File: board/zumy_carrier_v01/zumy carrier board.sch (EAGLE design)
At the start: 17 parts, among them M1 POLOLU_STEP_DOWN, M2 ITG/MPU_MODULE, M3 POLOLU_DRV8833_MODULE, SW1 500SSP1S1M6QEA

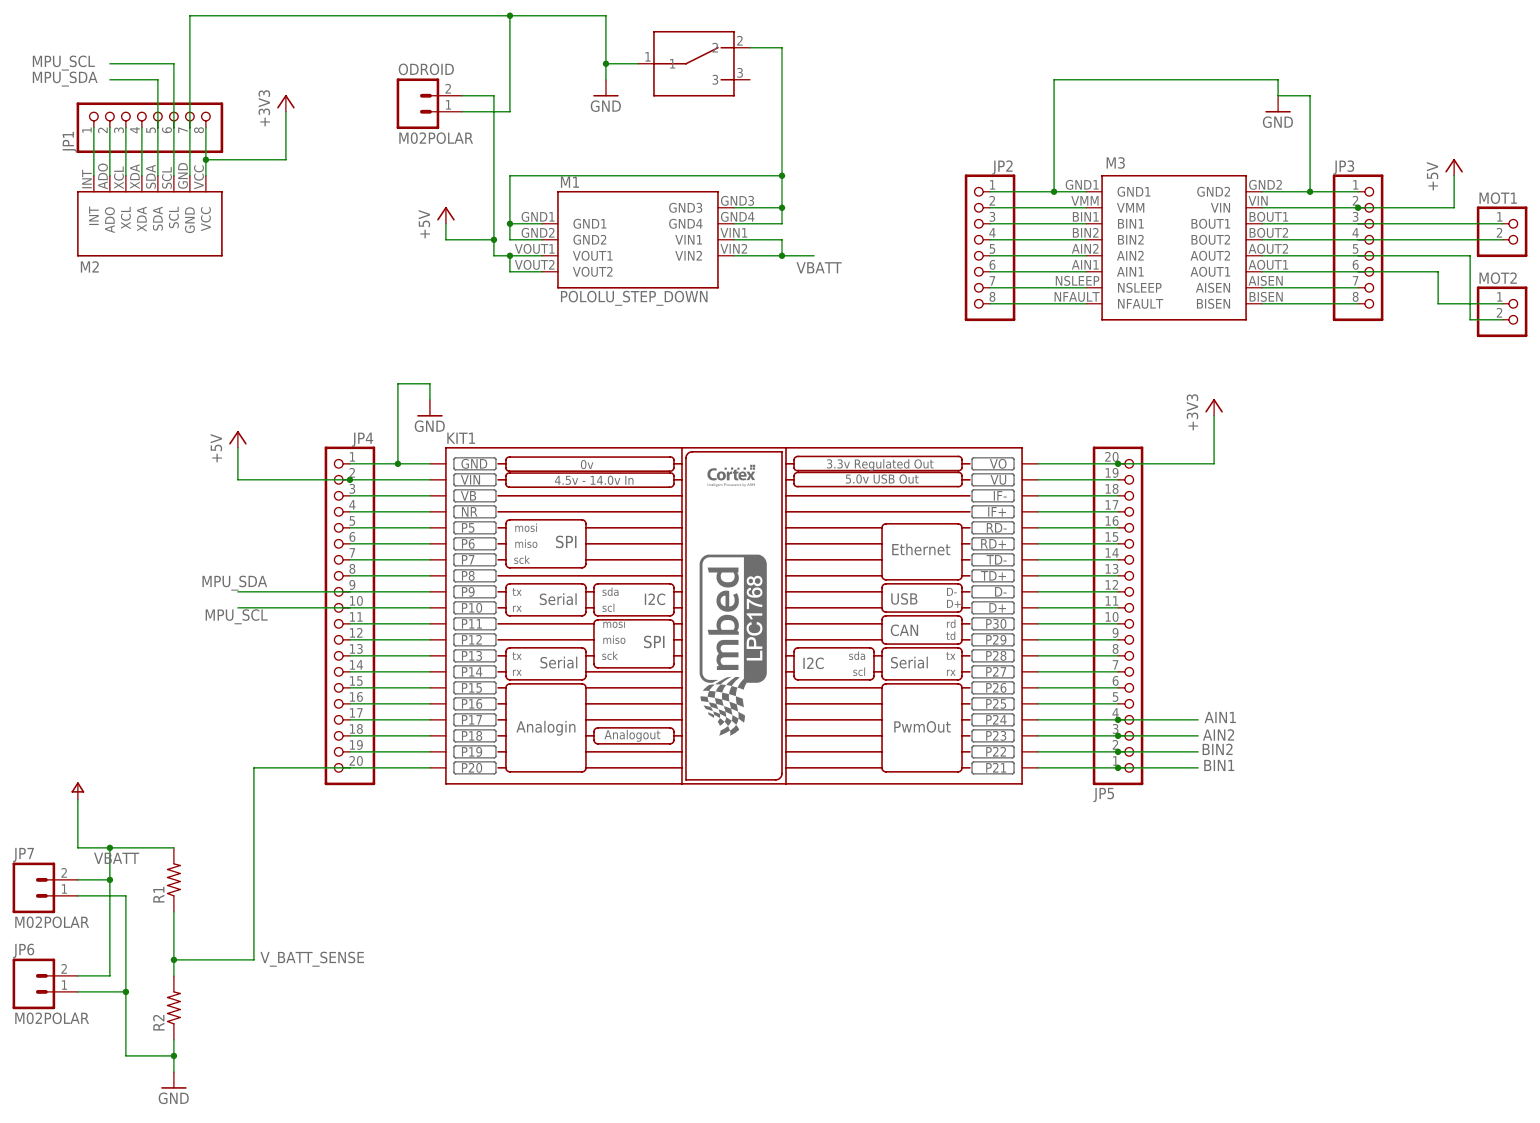
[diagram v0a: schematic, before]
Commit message: Preliminary updates for rev c, unrouted.
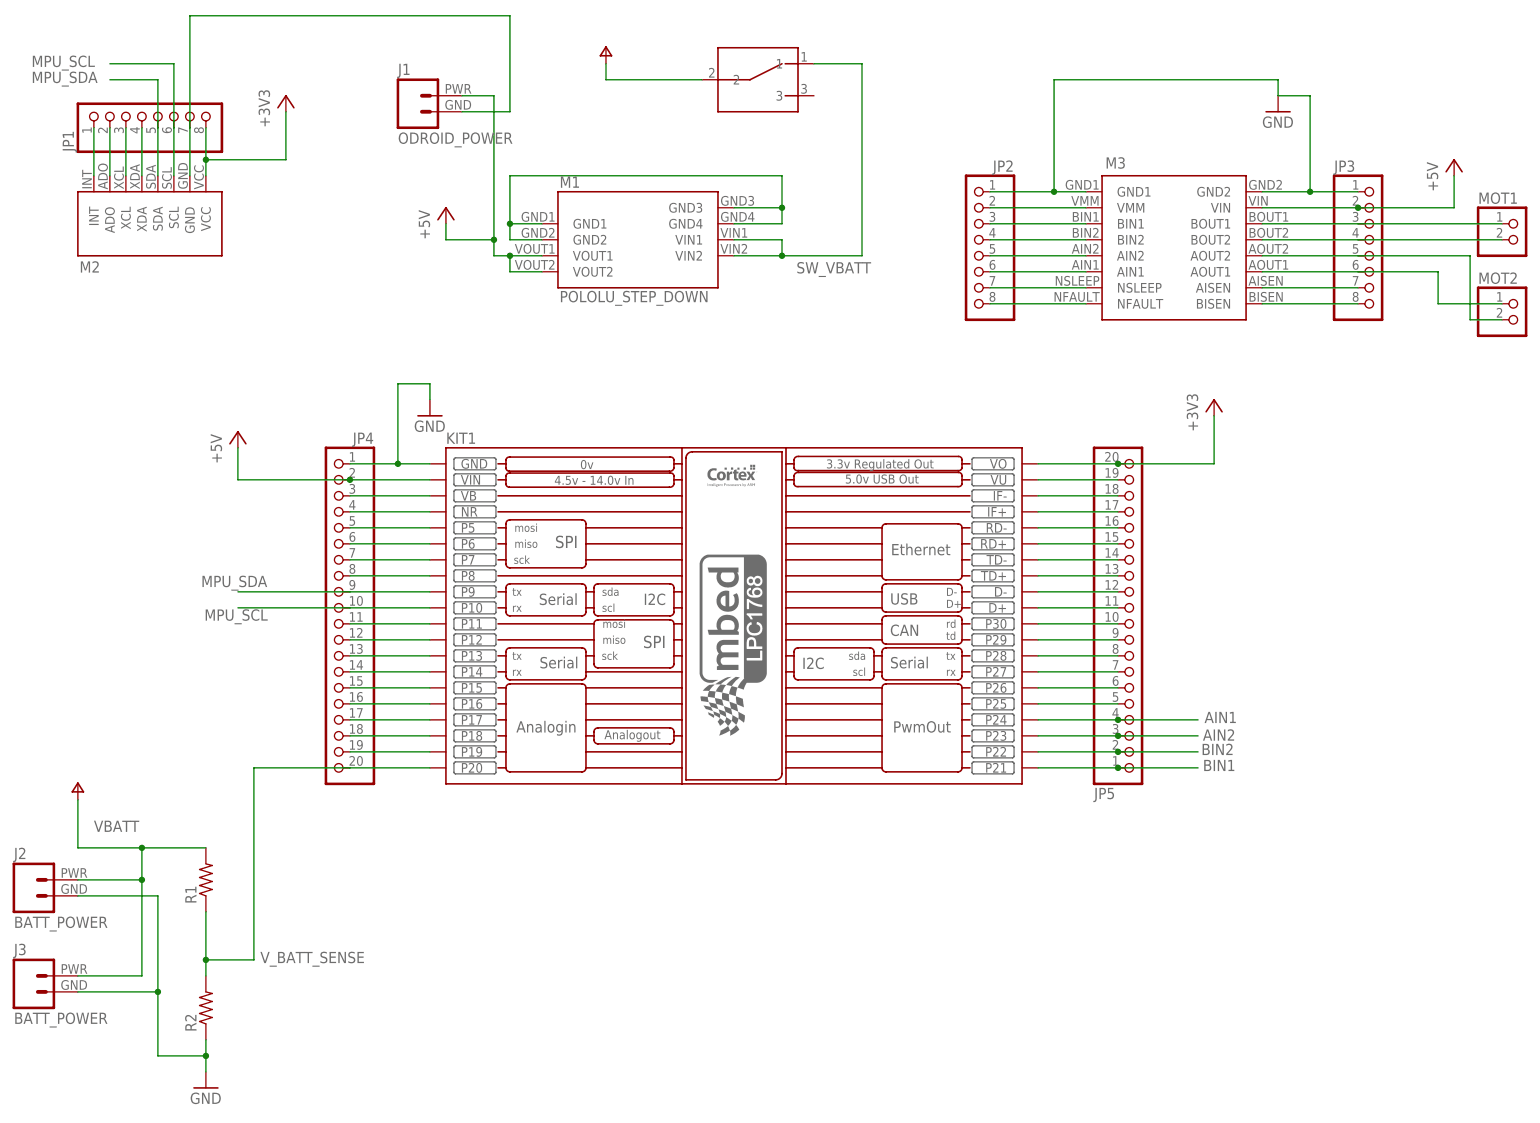
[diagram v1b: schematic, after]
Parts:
- removed JP6, JP7, ODROID: M02POLAR, SparkFun-Connectors:M02POLAR
- added J1: ODROID_POWER, zumy:ODROID_POWER
- added J2, J3: BATT_POWER, zumy:BATT_POWER
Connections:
- new net N$5: J1.GND, JP1.7, M2.GND
- new net SW_VBATT: M1.VIN1, M1.VIN2, SW1.1
- net +5V: now also J1.PWR; no longer ODROID.2
- net GND: now also J2.GND, J3.GND; no longer JP1.7, JP6.1, JP7.1, M2.GND, ODROID.1, SW1.1
- net N$65: no longer SW1.2
- net VBATT: now also J2.PWR, J3.PWR, SW1.2; no longer JP6.2, JP7.2, M1.VIN1, M1.VIN2
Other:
- moved on the sheet: R1, R2

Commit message: added rev c zumy carrier board
expanded odroid power holes
expanded battery power holes
module layout change
fixed switching cicuit to switch battery rather than ground
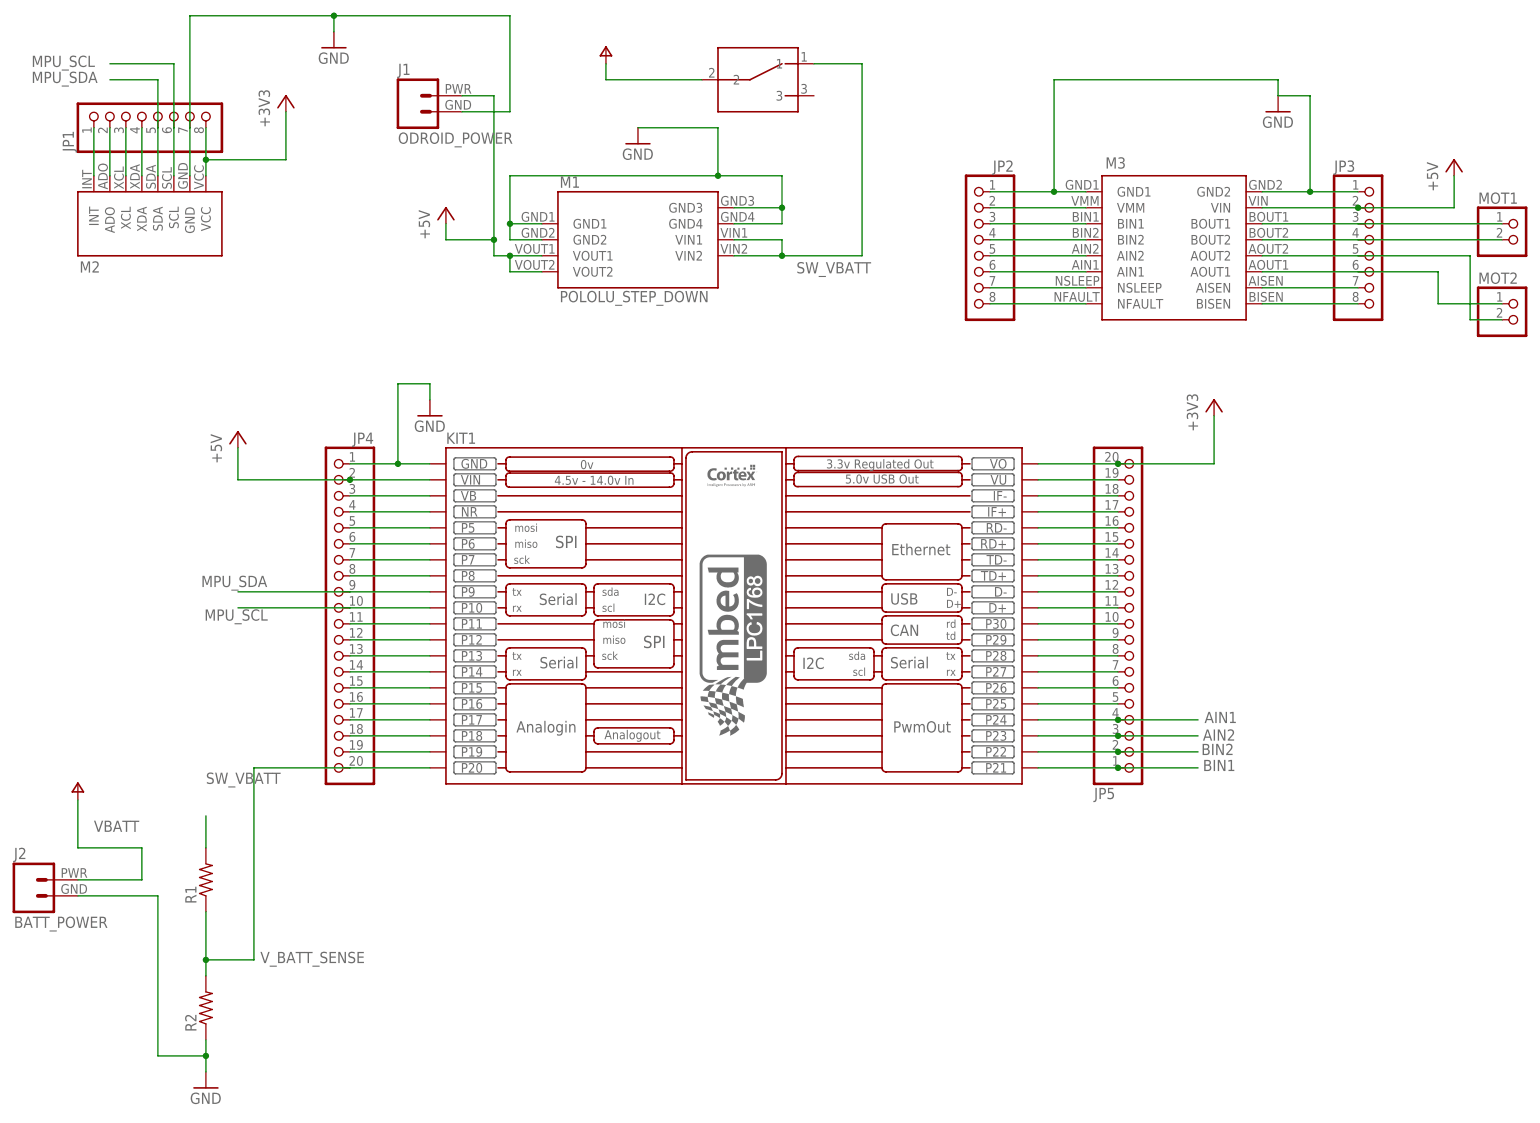
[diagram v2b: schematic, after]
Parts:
- removed J3: BATT_POWER, zumy:BATT_POWER
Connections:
- removed net N$5: J1.GND, JP1.7, M2.GND
- removed net N$65: M1.GND1, M1.GND2, M1.GND3, M1.GND4
- net GND: now also J1.GND, JP1.7, M1.GND1, M1.GND2, M1.GND3, M1.GND4, M2.GND; no longer J3.GND
- net SW_VBATT: now also R1.2
- net VBATT: no longer J3.PWR, R1.2
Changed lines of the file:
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@@
 <?xml version="1.0" encoding="utf-8"?>
 <!DOCTYPE eagle SYSTEM "eagle.dtd">
-<eagle version="6.5.0">
+<eagle version="6.6.0">
 <drawing>
 <settings>
@@
 <part name="P+5" library="supply1" deviceset="V+" device=""/>
 <part name="J2" library="zumy" deviceset="BATT_POWER" device=""/>
-<part name="J3" library="zumy" deviceset="BATT_POWER" device=""/>
+<part name="GND3" library="supply1" deviceset="GND" device=""/>
+<part name="GND5" library="supply1" deviceset="GND" device=""/>
 </parts>
 <sheets>
@@
 <instance part="P+5" gate="1" x="99.06" y="172.72" smashed="yes"/>
 <instance part="J2" gate="G$1" x="5.08" y="35.56"/>
-<instance part="J3" gate="G$1" x="5.08" y="20.32"/>
+<instance part="GND3" gate="1" x="104.14" y="157.48"/>
+<instance part="GND5" gate="1" x="55.88" y="172.72"/>
 </instances>
 <busses>
@@
 <pinref part="JP3" gate="A" pin="8"/>
 <wire x1="203.2" y1="132.08" x2="218.44" y2="132.08" width="0.1524" layer="91"/>
-</segment>
-</net>
-<net name="N$65" class="0">
-<segment>
-<pinref part="M1" gate="G$1" pin="GND3"/>
-<wire x1="127" y1="152.4" x2="127" y2="147.32" width="0.1524" layer="91"/>
-<wire x1="127" y1="147.32" x2="119.38" y2="147.32" width="0.1524" layer="91"/>
-<wire x1="127" y1="147.32" x2="127" y2="144.78" width="0.1524" layer="91"/>
-<pinref part="M1" gate="G$1" pin="GND4"/>
-<wire x1="127" y1="144.78" x2="119.38" y2="144.78" width="0.1524" layer="91"/>
-<junction x="127" y="147.32"/>
-<pinref part="M1" gate="G$1" pin="GND1"/>
-<wire x1="88.9" y1="144.78" x2="83.82" y2="144.78" width="0.1524" layer="91"/>
-<pinref part="M1" gate="G$1" pin="GND2"/>
-<wire x1="88.9" y1="142.24" x2="83.82" y2="142.24" width="0.1524" layer="91"/>
-<wire x1="83.82" y1="142.24" x2="83.82" y2="144.78" width="0.1524" layer="91"/>
-<wire x1="83.82" y1="144.78" x2="83.82" y2="152.4" width="0.1524" layer="91"/>
-<wire x1="83.82" y1="152.4" x2="127" y2="152.4" width="0.1524" layer="91"/>
-<junction x="83.82" y="144.78"/>
 </segment>
 </net>
@@
 <pinref part="GND1" gate="1" pin="GND"/>
 <wire x1="35.56" y1="12.7" x2="35.56" y2="10.16" width="0.1524" layer="91"/>
-<wire x1="15.24" y1="22.86" x2="27.94" y2="22.86" width="0.1524" layer="91"/>
-<wire x1="27.94" y1="22.86" x2="27.94" y2="12.7" width="0.1524" layer="91"/>
 <wire x1="27.94" y1="12.7" x2="35.56" y2="12.7" width="0.1524" layer="91"/>
 <junction x="35.56" y="12.7"/>
 <wire x1="15.24" y1="38.1" x2="27.94" y2="38.1" width="0.1524" layer="91"/>
-<wire x1="27.94" y1="38.1" x2="27.94" y2="22.86" width="0.1524" layer="91"/>
-<junction x="27.94" y="22.86"/>
+<wire x1="27.94" y1="38.1" x2="27.94" y2="12.7" width="0.1524" layer="91"/>
 <pinref part="J2" gate="G$1" pin="GND"/>
-<pinref part="J3" gate="G$1" pin="GND"/>
 </segment>
 <segment>
@@
 <junction x="170.18" y="149.86"/>
 </segment>
+<segment>
+<pinref part="M1" gate="G$1" pin="GND3"/>
+<wire x1="127" y1="152.4" x2="127" y2="147.32" width="0.1524" layer="91"/>
+<wire x1="127" y1="147.32" x2="119.38" y2="147.32" width="0.1524" layer="91"/>
+<wire x1="127" y1="147.32" x2="127" y2="144.78" width="0.1524" layer="91"/>
+<pinref part="M1" gate="G$1" pin="GND4"/>
+<wire x1="127" y1="144.78" x2="119.38" y2="144.78" width="0.1524" layer="91"/>
+<junction x="127" y="147.32"/>
+<pinref part="M1" gate="G$1" pin="GND1"/>
+<wire x1="88.9" y1="144.78" x2="83.82" y2="144.78" width="0.1524" layer="91"/>
+<pinref part="M1" gate="G$1" pin="GND2"/>
+<wire x1="88.9" y1="142.24" x2="83.82" y2="142.24" width="0.1524" layer="91"/>
+<wire x1="83.82" y1="142.24" x2="83.82" y2="144.78" width="0.1524" layer="91"/>
+<wire x1="83.82" y1="144.78" x2="83.82" y2="152.4" width="0.1524" layer="91"/>
+<wire x1="83.82" y1="152.4" x2="116.84" y2="152.4" width="0.1524" layer="91"/>
+<junction x="83.82" y="144.78"/>
+<pinref part="GND3" gate="1" pin="GND"/>
+<wire x1="116.84" y1="152.4" x2="127" y2="152.4" width="0.1524" layer="91"/>
+<wire x1="104.14" y1="160.02" x2="116.84" y2="160.02" width="0.1524" layer="91"/>
+<wire x1="116.84" y1="160.02" x2="116.84" y2="152.4" width="0.1524" layer="91"/>
+<junction x="116.84" y="152.4"/>
+</segment>
+<segment>
+<pinref part="M2" gate="G$1" pin="GND"/>
+<pinref part="JP1" gate="A" pin="7"/>
+<wire x1="33.02" y1="152.4" x2="33.02" y2="160.02" width="0.1524" layer="91"/>
+<wire x1="33.02" y1="160.02" x2="33.02" y2="177.8" width="0.1524" layer="91"/>
+<wire x1="33.02" y1="177.8" x2="55.88" y2="177.8" width="0.1524" layer="91"/>
+<wire x1="55.88" y1="177.8" x2="83.82" y2="177.8" width="0.1524" layer="91"/>
+<wire x1="83.82" y1="162.56" x2="76.2" y2="162.56" width="0.1524" layer="91"/>
+<wire x1="83.82" y1="162.56" x2="83.82" y2="177.8" width="0.1524" layer="91"/>
+<pinref part="J1" gate="G$1" pin="GND"/>
+<pinref part="GND5" gate="1" pin="GND"/>
+<wire x1="55.88" y1="175.26" x2="55.88" y2="177.8" width="0.1524" layer="91"/>
+<junction x="55.88" y="177.8"/>
+</segment>
 </net>
 <net name="VBATT" class="0">
 <segment>
-<pinref part="R1" gate="G$1" pin="2"/>
-<wire x1="35.56" y1="45.72" x2="25.4" y2="45.72" width="0.1524" layer="91"/>
 <wire x1="25.4" y1="45.72" x2="15.24" y2="45.72" width="0.1524" layer="91"/>
 <wire x1="15.24" y1="45.72" x2="15.24" y2="53.34" width="0.1524" layer="91"/>
 <pinref part="P+1" gate="1" pin="V+"/>
 <label x="17.78" y="48.26" size="1.778" layer="95"/>
-<wire x1="15.24" y1="25.4" x2="25.4" y2="25.4" width="0.1524" layer="91"/>
-<wire x1="25.4" y1="25.4" x2="25.4" y2="40.64" width="0.1524" layer="91"/>
-<junction x="25.4" y="45.72"/>
 <wire x1="25.4" y1="40.64" x2="25.4" y2="45.72" width="0.1524" layer="91"/>
 <wire x1="15.24" y1="40.64" x2="25.4" y2="40.64" width="0.1524" layer="91"/>
-<junction x="25.4" y="40.64"/>
 <pinref part="J2" gate="G$1" pin="PWR"/>
-<pinref part="J3" gate="G$1" pin="PWR"/>
 </segment>
 <segment>
@@
 </segment>
 </net>
-<net name="N$5" class="0">
-<segment>
-<pinref part="M2" gate="G$1" pin="GND"/>
-<pinref part="JP1" gate="A" pin="7"/>
-<wire x1="33.02" y1="152.4" x2="33.02" y2="160.02" width="0.1524" layer="91"/>
-<wire x1="33.02" y1="160.02" x2="33.02" y2="177.8" width="0.1524" layer="91"/>
-<wire x1="33.02" y1="177.8" x2="83.82" y2="177.8" width="0.1524" layer="91"/>
-<wire x1="83.82" y1="162.56" x2="76.2" y2="162.56" width="0.1524" layer="91"/>
-<wire x1="83.82" y1="162.56" x2="83.82" y2="177.8" width="0.1524" layer="91"/>
-<pinref part="J1" gate="G$1" pin="GND"/>
-</segment>
-</net>
 <net name="SW_VBATT" class="0">
 <segment>
@@
 <junction x="127" y="139.7"/>
 </segment>
-</net>
+<segment>
+<pinref part="R1" gate="G$1" pin="2"/>
+<wire x1="35.56" y1="45.72" x2="35.56" y2="50.8" width="0.1524" layer="91"/>
+<label x="35.56" y="55.88" size="1.778" layer="95"/>
+</segment>
+</net>
